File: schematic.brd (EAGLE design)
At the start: 70 x 25 mm, 3 parts, among them IC1 MEGA8-AI

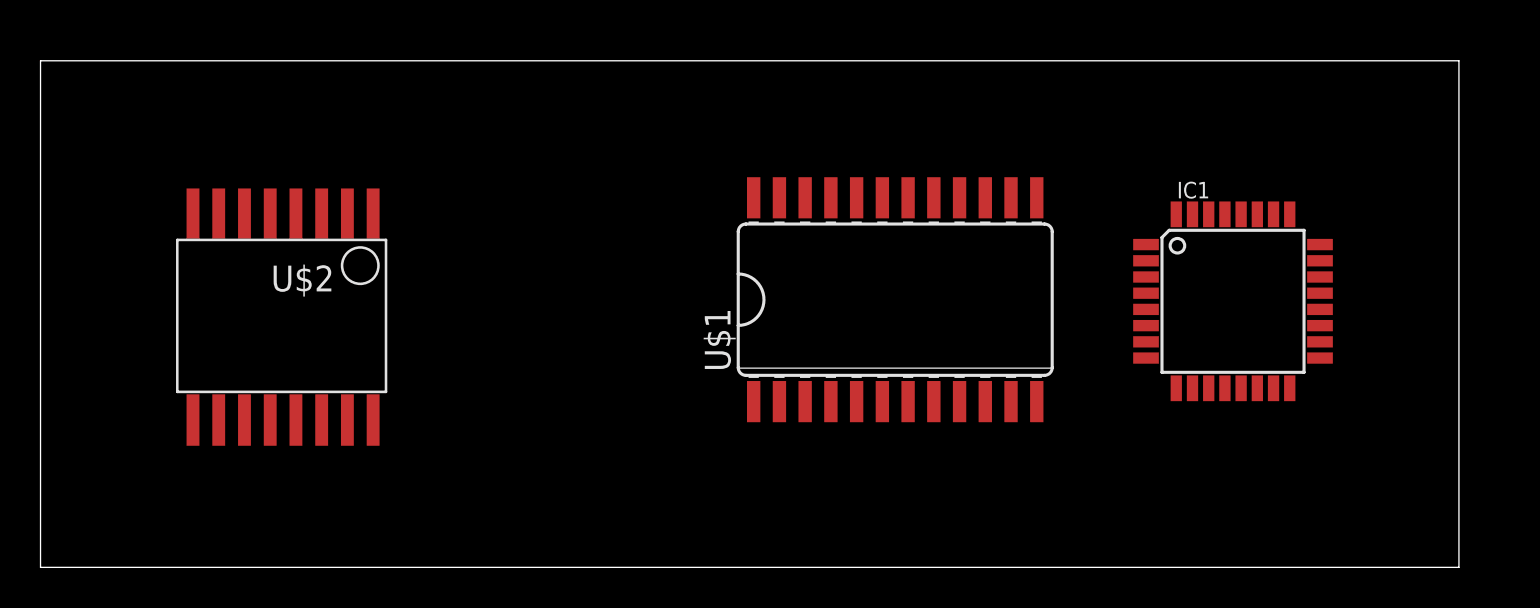
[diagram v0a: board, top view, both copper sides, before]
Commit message: Added LED and STM32
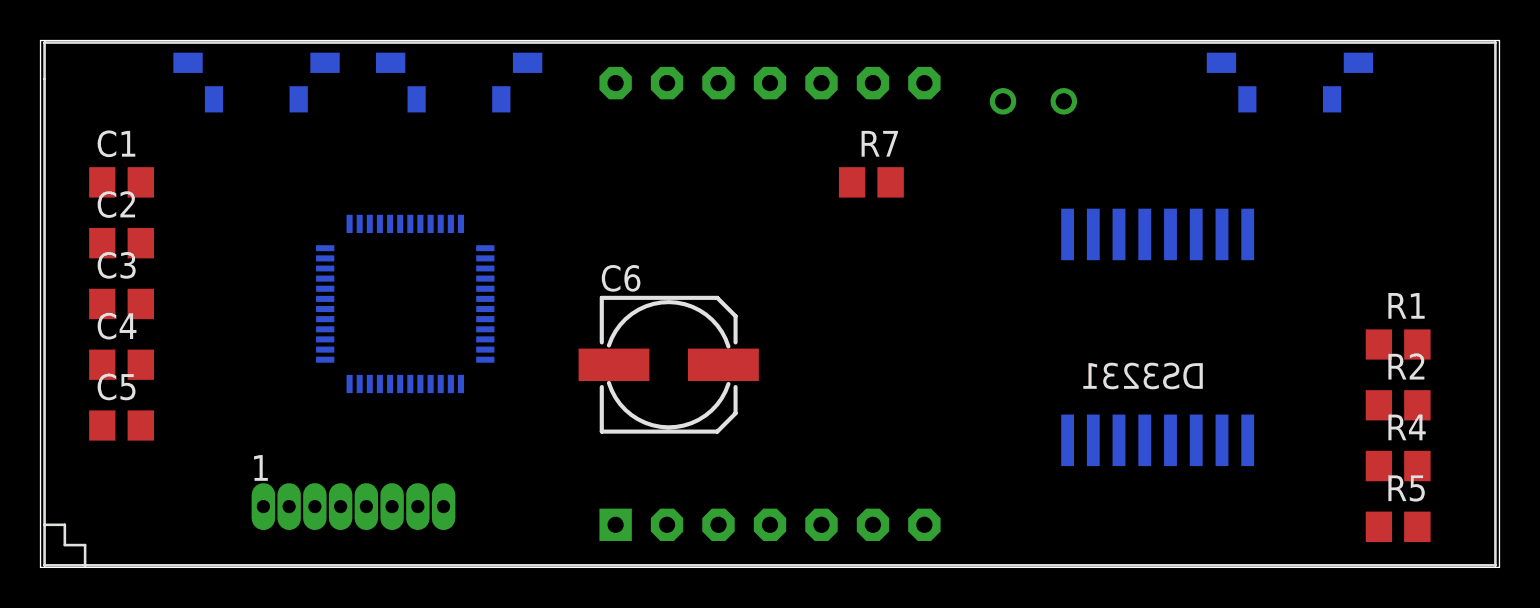
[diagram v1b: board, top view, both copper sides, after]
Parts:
- removed IC1: MEGA8-AI, atmel:TQFP32-08
- added C1, C2, C3, C4, C5: (no value), resistor:C0805
- added C6: (no value), resistor:153CLV-0605
- added JP1: (no value), PLL:PLL1.27-1X8
- added R1, R2, R4, R5, R7: (no value), resistor:R0805
- added U$3, U$4, U$5: IT1188E, misc:IT1188E
- added U$6: GL5537, misc:GL55
- added U$7: STM32F103C8, stm32:LQFP48-7X7
- U$1: value MAX7219CWG -> LBT8402BW; device max7219:SO24L -> lbt8402:LBT8402
- moved U$1 44.0 mm to (0.20, 0.10)
- moved U$2 33.0 mm to (50.0, 15.2), flipped to the bottom
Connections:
- new net +5V: C6.+
- new net AVCC: U$7.9
- new net N$2: JP1.3, U$7.37
- new net N$3: JP1.4, U$7.38
- new net N$5: JP1.6, U$7.40
- new net PHOTO_SENSOR: C5.1, R7.2, U$6.P$1
- new net SQW: R4.1, U$2.1
- new net TIMER_INT: R5.1, U$2.3
- new net VBAT: U$7.1
- net GND: now also C1.2, C2.2, C3.2, C4.2, C5.2, C6.-, R7.1, U$7.23, U$7.35, U$7.47, U$7.8; no longer IC1.21, IC1.3, IC1.5, U$1.4, U$1.9
- net N$1: now also JP1.2, U$7.34; no longer U$2.3
- net N$4: now also JP1.5, U$7.39; no longer U$2.1
- net RST: no longer IC1.29
- net SCL: now also R2.1; no longer IC1.28
- net SDA: now also R1.1; no longer IC1.27
- net VCC: now also C1.1, C2.1, C3.1, C4.1, R1.2, R2.2, R4.2, R5.2, U$6.P$2, U$7.24, U$7.36, U$7.48; no longer IC1.18, IC1.20, IC1.4, IC1.6, U$1.19
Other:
- board size 70 x 25 mm -> 72 x 26 mm

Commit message: .
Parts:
- removed JP1: (no value), PLL:PLL1.27-1X8
- added IC1: MEGA8-AI, atmel:TQFP32-08
- added R3: (no value), resistor:R0805
- added U$8: MICRO-USB, microusb:MICRO-USB
- added U$9: PINHD-1X5, PLL:PLL1.27-1X5
- U$7: value STM32F103C8 -> MAX7219CWG; device stm32:LQFP48-7X7 -> max7219:SO24L
- moved C5 54.4 mm to (56.0, 23.0), flipped to the bottom, turned to 180 degrees
- moved C1 52.0 mm to (56.0, 17.0), flipped to the bottom, turned to 180 degrees
- moved C3 40.9 mm to (42.0, 28.0), flipped to the bottom
- moved C2 22.2 mm to (26.0, 13.0), turned to 90 degrees
- moved C6 19.9 mm to (12.0, 4.00), flipped to the bottom, turned to 180 degrees
- moved R1 19.9 mm to (48.0, 5.00), flipped to the bottom, turned to 180 degrees
- moved R2 19.9 mm to (48.0, 2.00), flipped to the bottom, turned to 180 degrees
- moved R5 16.3 mm to (56.0, 14.0), flipped to the bottom, turned to 180 degrees
- moved R7 15.0 mm to (56.0, 20.0), flipped to the bottom
- moved U$7 14.0 mm to (32.0, 13.0), flipped to the top, turned to 180 degrees
- moved R4 12.5 mm to (56.0, 11.0), flipped to the bottom, turned to 180 degrees
- moved U$2 8.25 mm to (42.0, 17.2)
- moved C4 4.00 mm to (8.00, 10.0), flipped to the bottom, turned to 90 degrees
- moved U$5 2.00 mm to (61.0, 24.0)
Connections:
- net VBAT renamed DSP_DIN
- removed net +5V: C6.+
- removed net AVCC: U$7.9
- removed net RST: U$2.4
- new net DIG_1: U$1.P$14, U$7.14
- new net DSP_CLK: U$7.13
- new net DSP_LOAD: U$7.12
- new net MISO: IC1.16, U$9.2
- new net MOSI: IC1.15, U$9.1
- new net N$10: U$1.P$12, U$7.3
- new net N$11: U$1.P$5, U$7.10
- new net N$12: U$1.P$3, U$7.5
- new net N$13: U$1.P$1, U$1.P$8, U$7.8
- new net N$6: U$1.P$13, U$7.2
- new net N$7: U$1.P$9, U$7.11
- new net N$8: U$1.P$4, U$7.6
- new net N$9: U$1.P$2, U$7.7
- new net RESET: IC1.29, U$2.4, U$9.4
- new net SCK: IC1.17, U$9.3
- net GND: now also IC1.21, IC1.3, IC1.5, U$7.4, U$7.9, U$8.5, U$8.GND1, U$8.GND2, U$9.5; no longer U$7.23, U$7.35, U$7.47, U$7.8
- net N$1: now also R3.2, U$7.18; no longer JP1.2, U$7.34
- net N$2: now also U$1.P$11, U$7.16; no longer JP1.3, U$7.37
- net N$3: now also U$1.P$10, U$7.20; no longer JP1.4, U$7.38
- net N$4: now also U$1.P$6, U$7.23; no longer JP1.5, U$7.39
- net N$5: now also U$1.P$7, U$7.21; no longer JP1.6, U$7.40
- net SCL: now also IC1.28
- net SDA: now also IC1.27
- net VCC: now also C6.+, IC1.18, IC1.20, IC1.4, IC1.6, R3.1, U$7.19, U$8.1; no longer U$7.24, U$7.36, U$7.48

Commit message: .
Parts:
- added R6, R8, R9: (no value), resistor:R0805
- moved U$5 31.8 mm to (33.0, 39.0)
- moved U$3 15.8 mm to (13.0, 39.0)
- moved U$4 15.8 mm to (23.0, 39.0)
- moved C6 15.3 mm to (4.00, 17.0), turned to 90 degrees
- moved U$9 5.00 mm to (18.0, 2.00)
- moved C4 4.00 mm to (8.00, 6.00)
- moved U$8 3.00 mm to (0.00, 6.00)
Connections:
- new net BTN_1: R6.1, U$3.4
- new net BTN_2: R8.1, U$4.4
- new net BTN_3: R9.1, U$5.4
- net GND: now also U$3.3, U$4.3, U$5.3
- net VCC: now also R6.2, R8.2, R9.2

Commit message: Element placement
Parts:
- removed C6: (no value), resistor:153CLV-0605
- removed R9: (no value), resistor:R0805
- removed U$5: IT1188E, misc:IT1188E
- added B1: BATTERY1220, Battery&Holder:1220-SMD
- moved R8 46.2 mm to (11.0, 20.0)
- moved R6 43.0 mm to (17.0, 20.0)
- moved R4 34.0 mm to (23.0, 3.00)
- moved R1 29.2 mm to (23.0, 20.0)
- moved R2 29.2 mm to (23.0, 17.0)
- moved R5 27.7 mm to (29.0, 20.0)
- moved C2 24.6 mm to (48.0, 2.00), flipped to the bottom, turned to 0 degrees
- moved U$4 21.9 mm to (7.00, 24.0)
- moved C1 21.2 mm to (35.0, 20.0)
- moved U$7 21.1 mm to (53.0, 11.0), turned to 0 degrees
- moved R3 20.6 mm to (48.0, 21.0), flipped to the bottom, turned to 180 degrees
- moved U$9 19.8 mm to (4.00, 16.0), turned to 90 degrees
- moved U$3 15.8 mm to (18.0, 24.0)
- moved U$2 15.6 mm to (30.1, 7.16), turned to 90 degrees
- moved C3 7.21 mm to (48.0, 24.0), turned to 180 degrees
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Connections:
- removed net BTN_3: R9.1, U$5.4
- new net N$14: B1.+, U$2.14
- net BTN_1: now also IC1.24
- net BTN_2: now also IC1.25
- net DSP_CLK: now also IC1.12
- net DSP_DIN: now also IC1.14
- net DSP_LOAD: now also IC1.13
- net GND: now also B1.-; no longer C6.-, U$5.3
- net PHOTO_SENSOR: now also IC1.23
- net SQW: now also IC1.32
- net TIMER_INT: now also IC1.1
- net VCC: no longer C6.+, R9.2

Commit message: PCB v1
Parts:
- added C6, C7, C8: 10uF, SparkFun-Capacitors:EIA3216
- added R9: 4.7k, resistor:R0805
- C1, C2, C3, C4, C5: value (none) -> 0.1
- R1, R2, R4, R5, R6, R8: value (none) -> 4.7k
- R3: value (none) -> 10k
- R7: value (none) -> 68k
- moved R3 11.7 mm to (54.0, 11.0), turned to 270 degrees
- moved U$3 11.0 mm to (7.00, 24.0)
- moved U$4 11.0 mm to (18.0, 24.0)
- moved C2 9.49 mm to (51.0, 11.0), turned to 270 degrees
- moved R6 9.06 mm to (8.00, 19.0), turned to 270 degrees
- moved C4 5.10 mm to (13.0, 2.00), turned to 180 degrees
- moved C5 2.83 mm to (61.0, 23.0), turned to 90 degrees
- moved U$2 2.24 mm to (29.1, 5.16)
- moved C1 2.00 mm to (33.0, 20.0)
- moved R7 1.41 mm to (58.0, 23.0), turned to 270 degrees
- moved B1 1.00 mm to (63.9, 12.6)
- moved C3 1.00 mm to (48.0, 23.0), turned to 90 degrees
- moved R4 1.00 mm to (23.0, 2.00), turned to 0 degrees
- moved R5 1.00 mm to (28.0, 20.0)
- moved R8 1.00 mm to (11.0, 19.0), turned to 270 degrees
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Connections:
- new net USB_D+: U$8.3
- new net USB_D-: U$8.2
- net GND: now also C6.C, C7.C
- net PHOTO_SENSOR: now also C8.C
- net RESET: now also R9.1
- net VCC: now also C6.A, C7.A, C8.A, R9.2
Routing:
- net GND: track 0.00 -> 168.9 mm, vias 0 -> 5
- net VCC: track 0.00 -> 139.0 mm, vias 0 -> 8
- net PHOTO_SENSOR: track 0.00 -> 53.0 mm, vias 0 -> 3
- net DSP_DIN: track 0.00 -> 52.6 mm, vias 0 -> 1
- net DSP_CLK: track 0.00 -> 52.3 mm, vias 0 -> 3
- net N$13: track 0.00 -> 49.7 mm, vias 0 -> 3
- net DSP_LOAD: track 0.00 -> 49.1 mm, vias 0 -> 3
- net RESET: track 0.00 -> 45.6 mm
- net SCL: track 0.00 -> 40.4 mm
- net TIMER_INT: track 0.00 -> 36.6 mm, vias 0 -> 2
- net DIG_1: track 0.00 -> 35.2 mm
- net N$6: track 0.00 -> 33.1 mm
- net N$10: track 0.00 -> 30.0 mm, vias 0 -> 1
- net N$7: track 0.00 -> 29.4 mm, vias 0 -> 1
- net SDA: track 0.00 -> 28.9 mm, vias 0 -> 2
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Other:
- board text added: "Clock (c) snakeye v1"

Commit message: PCB design
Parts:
- removed C3: 0.1, resistor:C0805
- removed C7: 10uF, SparkFun-Capacitors:EIA3216
- moved R5 15.8 mm to (23.0, 5.00), turned to 0 degrees
- moved C1 15.5 mm to (32.5, 4.50)
- moved C4 7.48 mm to (8.40, 7.90), turned to 90 degrees
- moved C6 7.07 mm to (15.7, 2.40), turned to 180 degrees
- moved R3 6.67 mm to (47.5, 12.5), turned to 180 degrees
- moved R9 5.83 mm to (23.0, 17.0), turned to 180 degrees
- moved U$7 5.30 mm to (47.7, 11.2)
- moved R1 4.50 mm to (18.5, 20.0)
- moved C2 3.81 mm to (47.5, 9.50), turned to 180 degrees
- moved R2 3.00 mm to (23.0, 20.0)
- moved C8 2.65 mm to (51.0, 19.7)
- moved C5 2.55 mm to (58.5, 22.5), turned to 270 degrees
- moved R7 2.55 mm to (55.5, 22.5), turned to 90 degrees
- moved U$6 2.55 mm to (51.0, 22.8)
- moved R6 2.50 mm to (9.50, 17.0), turned to 0 degrees
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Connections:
- net GND: no longer C3.2, C7.C
- net VCC: no longer C3.1, C7.A
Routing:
- net GND: track 168.9 -> 137.2 mm, vias 5 -> 4
- net N$13: track 49.7 -> 80.9 mm
- net TIMER_INT: track 36.6 -> 12.3 mm, vias 2 -> 0
- net DSP_DIN: track 52.6 -> 33.8 mm, vias 1 -> 3
- net RESET: track 45.6 -> 31.6 mm, vias 0 -> 1
- net SDA: track 28.9 -> 38.9 mm, vias 2 -> 3
- net N$12: track 27.0 -> 17.1 mm
- net N$14: track 27.7 -> 36.8 mm, vias 0 -> 2
- net N$6: track 33.1 -> 24.6 mm, vias 0 -> 2
- net SCL: track 40.4 -> 32.0 mm, vias 0 -> 2
- net N$10: track 30.0 -> 21.8 mm, vias 1 -> 2
- net BTN_2: track 17.1 -> 24.6 mm
- net N$3: track 17.9 -> 10.8 mm
- net DIG_1: track 35.2 -> 28.6 mm, vias 0 -> 1
- net N$5: track 17.4 -> 23.8 mm, vias 0 -> 1
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- added copper zone on layer 1, net GND
- added copper zone on layer 16, net GND
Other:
- board text removed: "Clock (c) snakeye v1"

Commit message: .
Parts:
- removed C1, C2, C4: 0.1, resistor:C0805
- removed C6: 10uF, SparkFun-Capacitors:EIA3216
- removed IC1: MEGA8-AI, atmel:TQFP32-08
- removed R6, R8: 4.7k, resistor:R0805
- removed U$3, U$4: IT1188E, misc:IT1188E
- removed U$9: PINHD-1X5, PLL:PLL1.27-1X5
- added U1: (no value), esp8266modules:ESP12E-SMD
- moved R4 63.9 mm to (55.5, 57.5)
- moved R5 56.4 mm to (41.0, 58.5)
- moved R3 47.4 mm to (3.50, 30.0)
- moved R9 39.2 mm to (30.5, 55.5)
- moved R2 36.7 mm to (19.0, 56.5)
- moved R1 34.0 mm to (10.5, 53.0)
- moved U$2 32.9 mm to (7.05, 32.2)
- moved U$7 30.1 mm to (30.2, 35.7)
- moved C5 27.5 mm to (80.5, 39.0)
- moved R7 25.6 mm to (75.5, 38.5)
- moved B1 23.6 mm to (61.0, 35.5)
- moved U$6 16.0 mm to (47.0, 38.3)
- moved C8 14.4 mm to (47.5, 33.7)
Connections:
- removed net BTN_1: IC1.24, R6.1, U$3.4
- removed net BTN_2: IC1.25, R8.1, U$4.4
- removed net MISO: IC1.16, U$9.2
- removed net MOSI: IC1.15, U$9.1
- removed net SCK: IC1.17, U$9.3
- removed net VCC: C1.1, C2.1, C4.1, C6.A, C8.A, IC1.18, IC1.20, IC1.4, IC1.6, R1.2, R2.2, R3.1, R4.2, R5.2, R6.2, R8.2, R9.2, U$2.2, U$6.P$2, U$7.19, U$8.1
- new net +3V3: C8.A, R1.2, R2.2, R4.2, R5.2, R9.2, U$2.2, U$6.P$2, U1.VCC
- new net +5V: R3.1, U$7.19, U$8.1
- new net RX: U1.RXD0
- new net TX: U1.TXD0
- net DSP_CLK: no longer IC1.12
- net DSP_DIN: no longer IC1.14
- net DSP_LOAD: no longer IC1.13
- net GND: now also U1.GND; no longer C1.2, C2.2, C4.2, C6.C, IC1.21, IC1.3, IC1.5, U$3.3, U$4.3, U$9.5
- net PHOTO_SENSOR: now also U1.ADC; no longer IC1.23
- net RESET: now also U1.RESET; no longer IC1.29, U$9.4
- net SCL: no longer IC1.28
- net SDA: no longer IC1.27
- net SQW: no longer IC1.32
- net TIMER_INT: no longer IC1.1
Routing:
- net VCC: track 145.1 -> 0.00 mm, vias 8 -> 0
- net GND: track 137.2 -> 0.00 mm, vias 4 -> 0
- net N$13: track 80.9 -> 0.00 mm, vias 3 -> 0
- net PHOTO_SENSOR: track 54.9 -> 0.00 mm, vias 2 -> 0
- net DSP_CLK: track 52.6 -> 0.00 mm, vias 3 -> 0
- net DSP_LOAD: track 50.7 -> 0.00 mm, vias 3 -> 0
- net SDA: track 38.9 -> 0.00 mm, vias 3 -> 0
- net N$14: track 36.8 -> 0.00 mm, vias 2 -> 0
- net DSP_DIN: track 33.8 -> 0.00 mm, vias 3 -> 0
- net SCL: track 32.0 -> 0.00 mm, vias 2 -> 0
- net RESET: track 31.6 -> 0.00 mm, vias 1 -> 0
- net DIG_1: track 28.6 -> 0.00 mm, vias 1 -> 0
- net BTN_2: track 24.6 -> 0.00 mm
- net N$6: track 24.6 -> 0.00 mm, vias 2 -> 0
- net N$9: track 24.5 -> 0.00 mm, vias 3 -> 0
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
